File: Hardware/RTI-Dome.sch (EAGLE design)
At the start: 32 parts, among them IC2 74LVC244

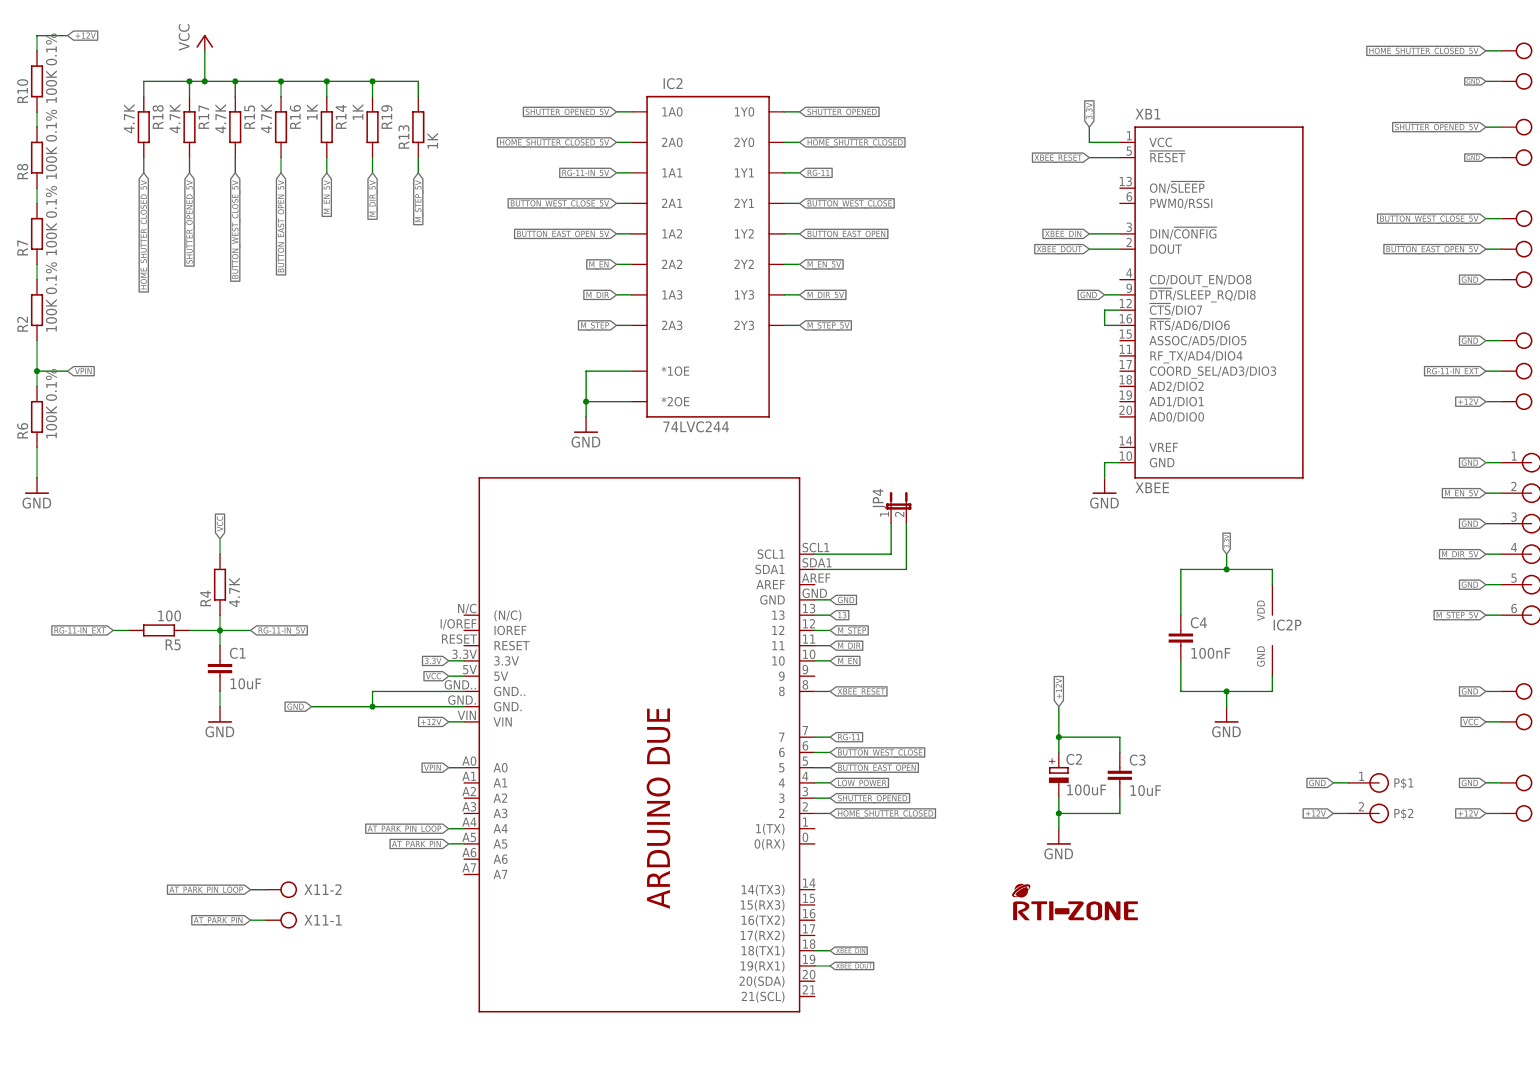
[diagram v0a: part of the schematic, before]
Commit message: Auto detect shutter presence.
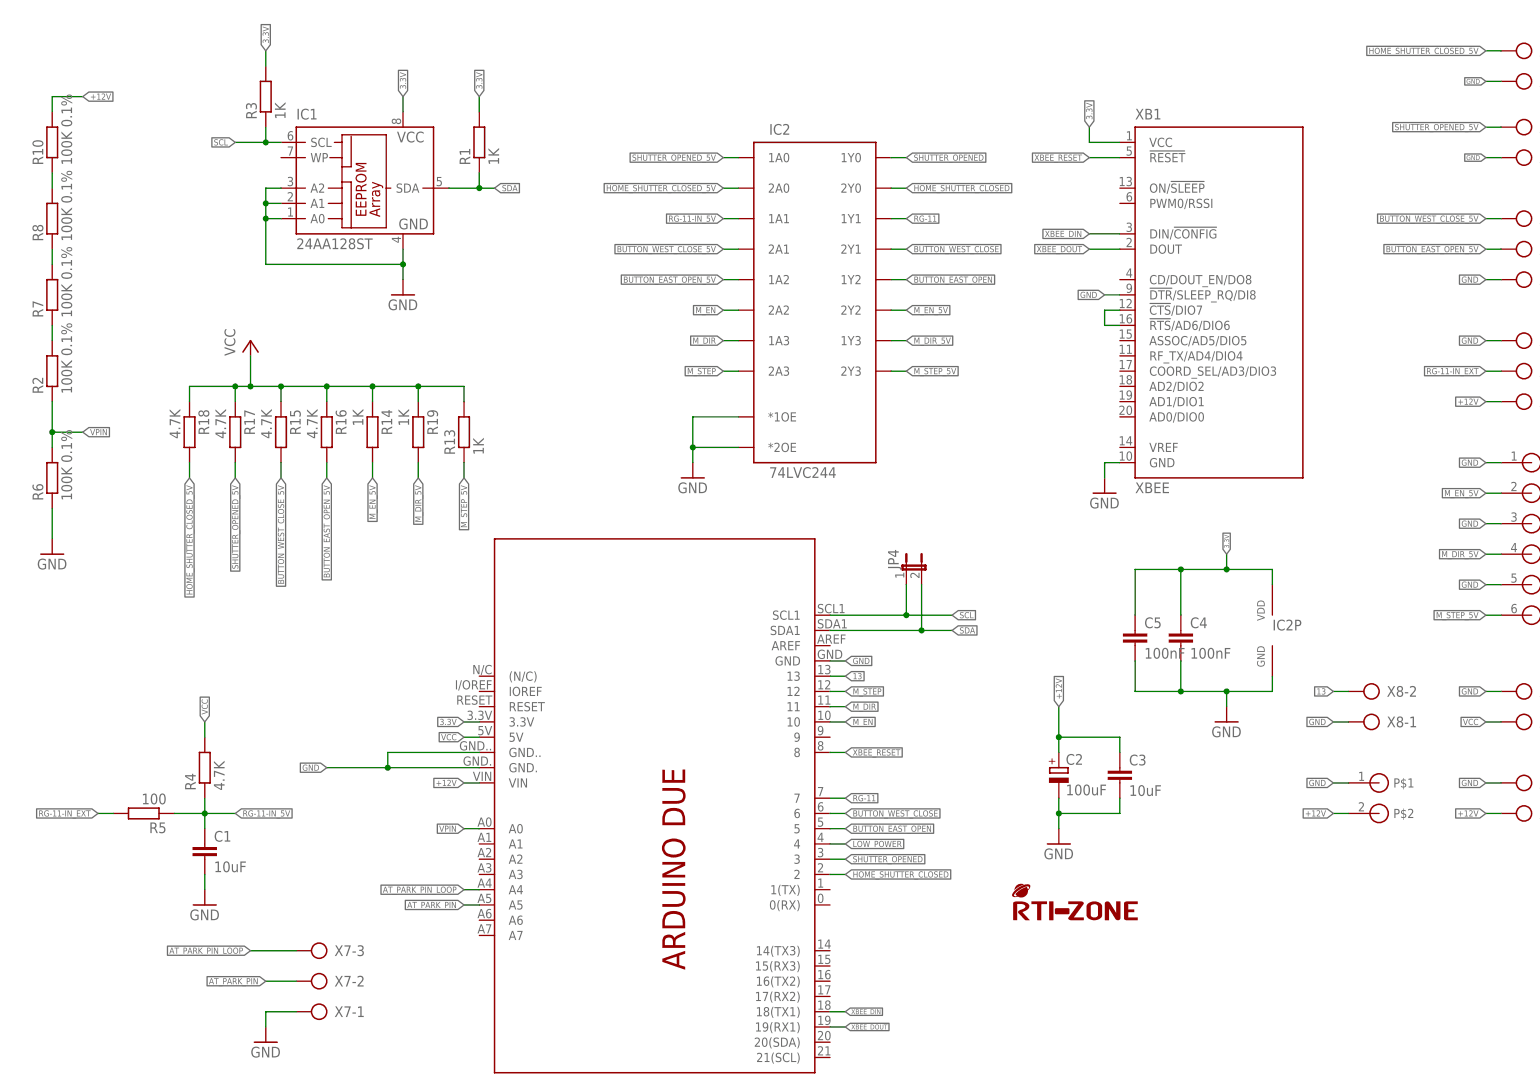
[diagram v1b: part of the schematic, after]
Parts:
- removed X11: (no value), con-ptr500:AK500/2
- added C5: 100nF, rti:C-EU'0805'
- added IC1: 24AA128ST, microchip:24AA128ST
- added R1, R3: 1K, rti:R-EU'0805'
- added X7: (no value), con-ptr500:AK500/3
- added X8: (no value), con-ptr500:AK500/2
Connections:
- removed net N$6: JP4.1, PCB1.SCL1
- removed net N$8: JP4.2, PCB1.SDA1
- new net SCL: IC1.SCL, JP4.1, PCB1.SCL1, R3.1
- new net SDA: IC1.SDA, JP4.2, PCB1.SDA1, R1.1
- net 13: now also X8-2.KL
- net 3.3V: now also C5.1, IC1.VCC, R1.2, R3.2
- net AT_PARK_PIN: now also X7-2.KL; no longer X11-1.KL
- net AT_PARK_PIN_LOOP: now also X7-3.KL; no longer X11-2.KL
- net GND: now also C5.2, IC1.A0, IC1.A1, IC1.A2, IC1.GND, X7-1.KL, X8-1.KL
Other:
- moved on the sheet: C1, IC2, JP4, R10, R13, R14, R15, R16, R17, R18, R19, R2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

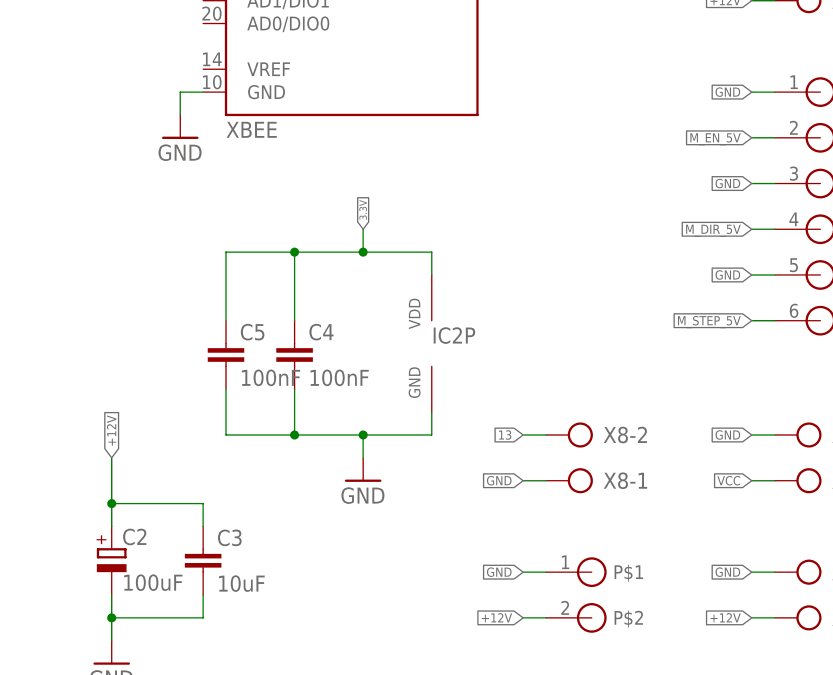
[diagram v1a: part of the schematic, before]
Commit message: Tested the ISD04 stepper controller.. needed to add 3.3V header as the pull-up on the buffer output don't bring the signal to 5V and therefore the optocoupler in the contoller doesn't do the right thing.
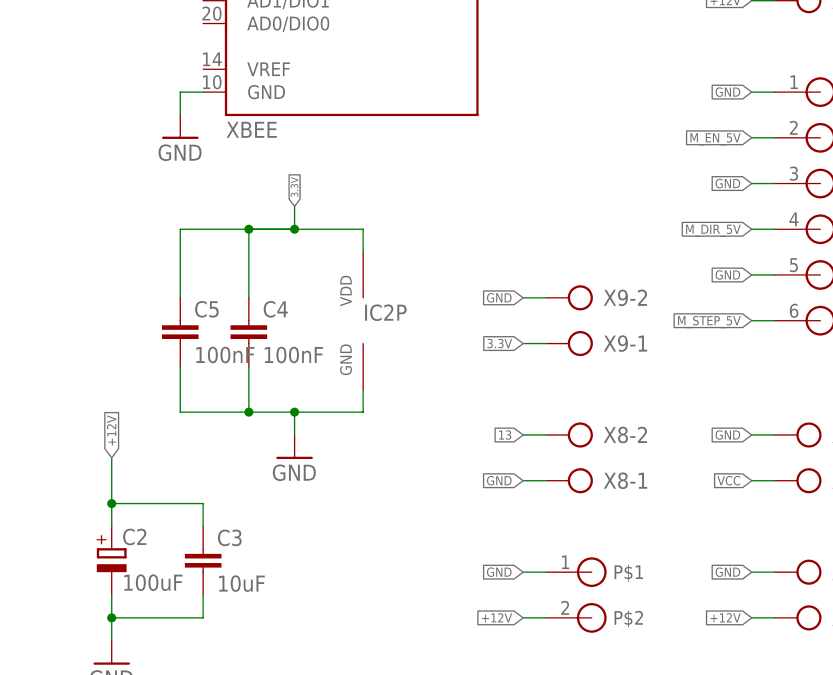
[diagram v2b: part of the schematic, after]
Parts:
- added X9: (no value), con-ptr500:AK500/2
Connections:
- net 3.3V: now also X9-1.KL
- net GND: now also X9-2.KL
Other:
- moved on the sheet: C4, C5, IC2P
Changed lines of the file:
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@@
 <part name="R3" library="rti" deviceset="R-EU" device="'0805'" value="1K"/>
 <part name="C5" library="rti" deviceset="C-EU" device="'0805'" value="100nF"/>
+<part name="X9" library="con-ptr500" deviceset="AK500/2" device=""/>
 </parts>
 <sheets>
@@
 <instance part="R8" gate="G$1" x="7.62" y="144.78" rot="R90"/>
 <instance part="R10" gate="G$1" x="7.62" y="157.48" rot="R90"/>
-<instance part="C4" gate="G$1" x="195.58" y="76.2"/>
-<instance part="IC2" gate="P" x="208.28" y="76.2" rot="R270"/>
-<instance part="GND1" gate="1" x="203.2" y="60.96"/>
+<instance part="C4" gate="G$1" x="190.5" y="78.74"/>
+<instance part="IC2" gate="P" x="200.66" y="78.74" rot="R270"/>
+<instance part="GND1" gate="1" x="195.58" y="63.5"/>
 <instance part="XB1" gate="G$1" x="200.66" y="132.08"/>
 <instance part="GND6" gate="1" x="182.88" y="99.06"/>
@@
 <instance part="R1" gate="G$1" x="78.74" y="157.48" rot="R90"/>
 <instance part="R3" gate="G$1" x="43.18" y="165.1" rot="R90"/>
-<instance part="C5" gate="G$1" x="187.96" y="76.2"/>
+<instance part="C5" gate="G$1" x="182.88" y="78.74"/>
+<instance part="X9" gate="-1" x="228.6" y="76.2" rot="R180"/>
+<instance part="X9" gate="-2" x="228.6" y="81.28" rot="R180"/>
 </instances>
 <busses>
@@
 </segment>
 <segment>
-<wire x1="195.58" y1="66.04" x2="203.2" y2="66.04" width="0.1524" layer="91"/>
-<wire x1="203.2" y1="66.04" x2="210.82" y2="66.04" width="0.1524" layer="91"/>
+<wire x1="190.5" y1="68.58" x2="195.58" y2="68.58" width="0.1524" layer="91"/>
+<wire x1="195.58" y1="68.58" x2="203.2" y2="68.58" width="0.1524" layer="91"/>
 <pinref part="IC2" gate="P" pin="GND"/>
-<wire x1="210.82" y1="68.58" x2="210.82" y2="66.04" width="0.1524" layer="91"/>
+<wire x1="203.2" y1="71.12" x2="203.2" y2="68.58" width="0.1524" layer="91"/>
 <pinref part="C4" gate="G$1" pin="2"/>
-<wire x1="195.58" y1="71.12" x2="195.58" y2="66.04" width="0.1524" layer="91"/>
-<wire x1="203.2" y1="66.04" x2="203.2" y2="63.5" width="0.1524" layer="91"/>
-<junction x="203.2" y="66.04"/>
+<wire x1="190.5" y1="73.66" x2="190.5" y2="68.58" width="0.1524" layer="91"/>
+<wire x1="195.58" y1="68.58" x2="195.58" y2="66.04" width="0.1524" layer="91"/>
+<junction x="195.58" y="68.58"/>
 <pinref part="GND1" gate="1" pin="GND"/>
 <pinref part="C5" gate="G$1" pin="2"/>
-<wire x1="195.58" y1="66.04" x2="187.96" y2="66.04" width="0.1524" layer="91"/>
-<wire x1="187.96" y1="66.04" x2="187.96" y2="71.12" width="0.1524" layer="91"/>
-<junction x="195.58" y="66.04"/>
+<wire x1="190.5" y1="68.58" x2="182.88" y2="68.58" width="0.1524" layer="91"/>
+<wire x1="182.88" y1="68.58" x2="182.88" y2="73.66" width="0.1524" layer="91"/>
+<junction x="190.5" y="68.58"/>
 </segment>
 <segment>
@@
 <junction x="66.04" y="137.16"/>
 </segment>
+<segment>
+<pinref part="X9" gate="-2" pin="KL"/>
+<wire x1="220.98" y1="81.28" x2="223.52" y2="81.28" width="0.1524" layer="91"/>
+<label x="220.98" y="81.28" size="1.016" layer="95" rot="R180" xref="yes"/>
+</segment>
 </net>
 <net name="+12V" class="1">
@@
 </segment>
 <segment>
-<wire x1="210.82" y1="86.36" x2="203.2" y2="86.36" width="0.1524" layer="91"/>
-<wire x1="203.2" y1="86.36" x2="195.58" y2="86.36" width="0.1524" layer="91"/>
+<wire x1="203.2" y1="88.9" x2="195.58" y2="88.9" width="0.1524" layer="91"/>
+<wire x1="195.58" y1="88.9" x2="190.5" y2="88.9" width="0.1524" layer="91"/>
 <pinref part="C4" gate="G$1" pin="1"/>
-<wire x1="195.58" y1="86.36" x2="195.58" y2="78.74" width="0.1524" layer="91"/>
+<wire x1="190.5" y1="88.9" x2="190.5" y2="81.28" width="0.1524" layer="91"/>
 <pinref part="IC2" gate="P" pin="VDD"/>
-<wire x1="210.82" y1="86.36" x2="210.82" y2="83.82" width="0.1524" layer="91"/>
-<wire x1="203.2" y1="86.36" x2="203.2" y2="88.9" width="0.1524" layer="91"/>
-<junction x="203.2" y="86.36"/>
-<label x="203.2" y="88.9" size="0.8128" layer="95" rot="R90" xref="yes"/>
+<wire x1="203.2" y1="88.9" x2="203.2" y2="86.36" width="0.1524" layer="91"/>
+<wire x1="195.58" y1="88.9" x2="195.58" y2="91.44" width="0.1524" layer="91"/>
+<junction x="195.58" y="88.9"/>
+<label x="195.58" y="91.44" size="0.8128" layer="95" rot="R90" xref="yes"/>
 <pinref part="C5" gate="G$1" pin="1"/>
-<wire x1="195.58" y1="86.36" x2="187.96" y2="86.36" width="0.1524" layer="91"/>
-<wire x1="187.96" y1="86.36" x2="187.96" y2="78.74" width="0.1524" layer="91"/>
-<junction x="195.58" y="86.36"/>
+<wire x1="190.5" y1="88.9" x2="182.88" y2="88.9" width="0.1524" layer="91"/>
+<wire x1="182.88" y1="88.9" x2="182.88" y2="81.28" width="0.1524" layer="91"/>
+<junction x="190.5" y="88.9"/>
+<wire x1="195.58" y1="88.9" x2="190.5" y2="88.9" width="0.1524" layer="91"/>
 </segment>
 <segment>
@@
 <label x="78.74" y="165.1" size="1.016" layer="95" rot="R90" xref="yes"/>
 </segment>
-</net>
+<segment>
+<pinref part="X9" gate="-1" pin="KL"/>
+<wire x1="220.98" y1="76.2" x2="223.52" y2="76.2" width="0.1524" layer="91"/>
+<label x="220.98" y="76.2" size="1.016" layer="95" rot="R180" xref="yes"/>
+</segment>
+</net>
